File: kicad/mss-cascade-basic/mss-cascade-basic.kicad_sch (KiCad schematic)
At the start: 75 parts, among them J1 Screw_Terminal_01x02, U1 AP7381-50Y

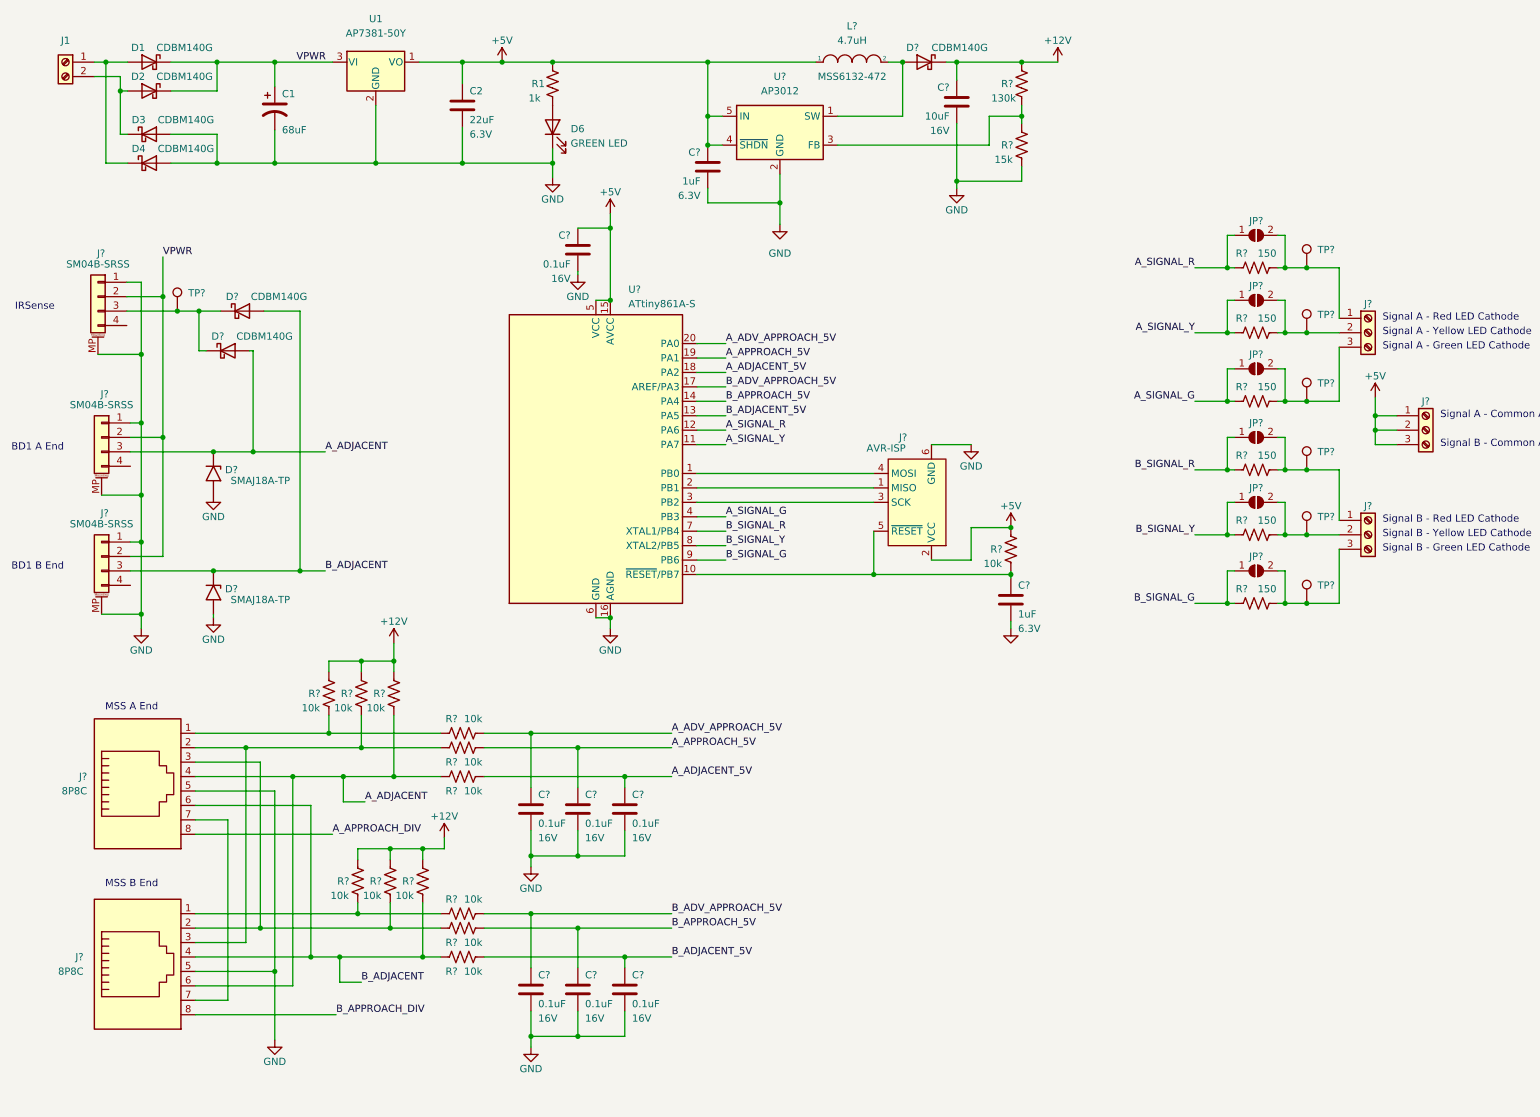
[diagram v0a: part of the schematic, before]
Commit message: Schematic updates and moving things around on the basic
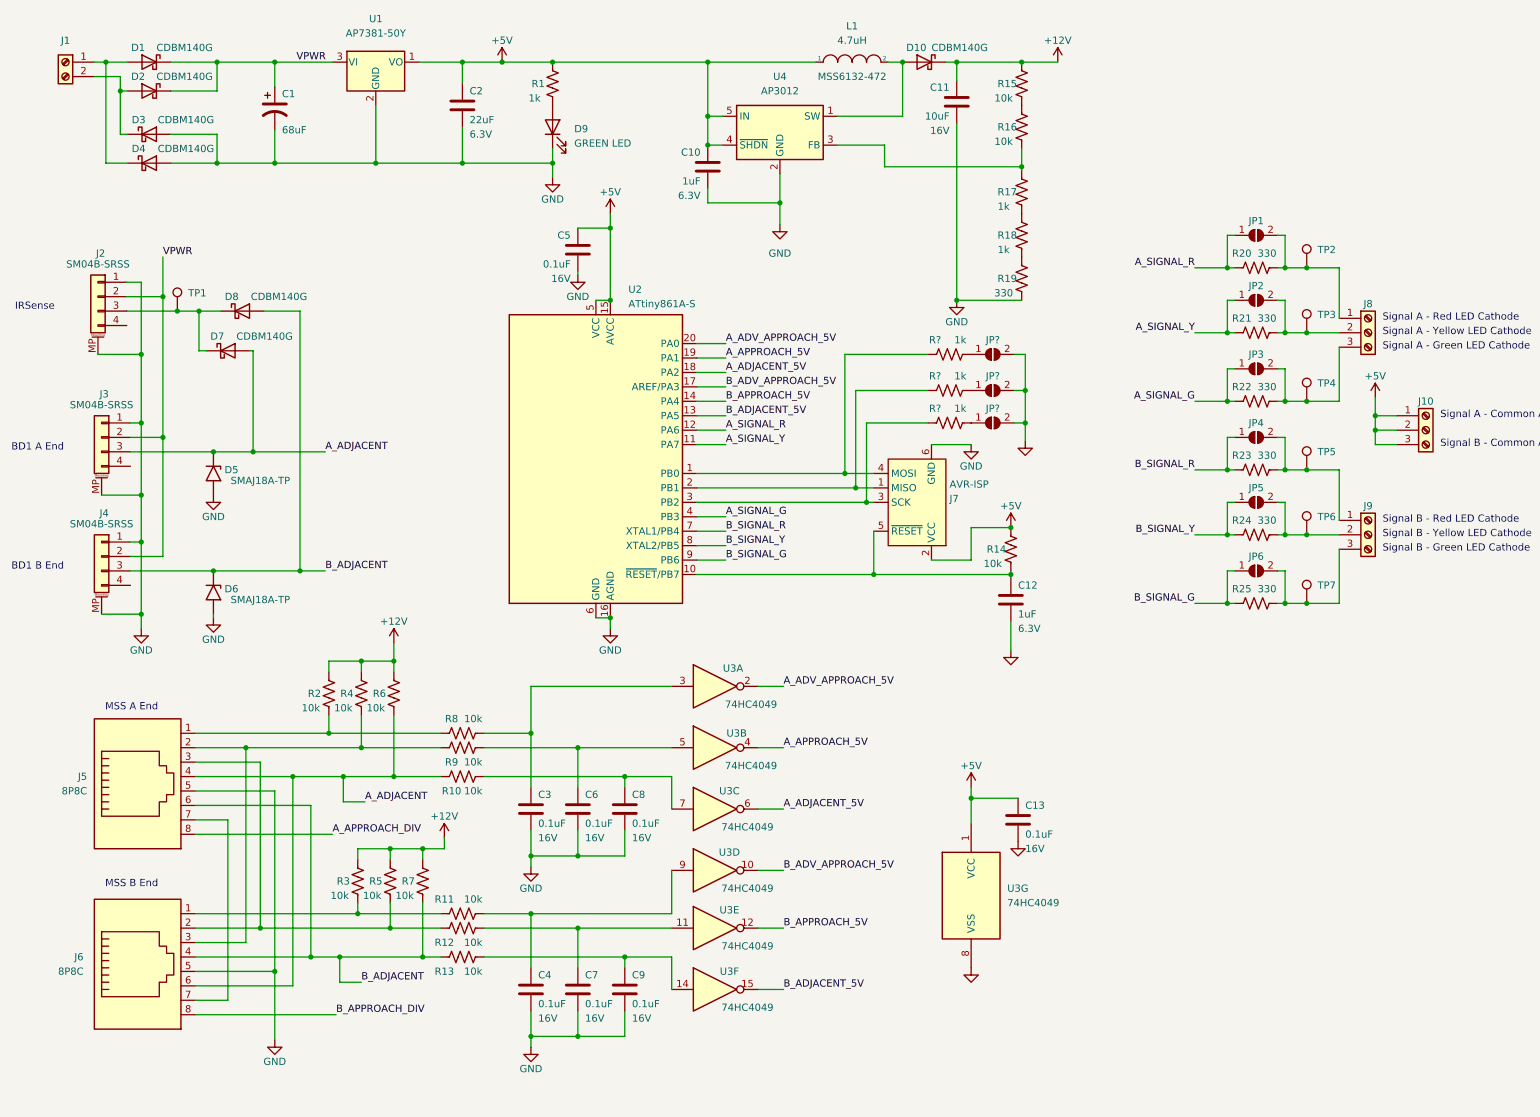
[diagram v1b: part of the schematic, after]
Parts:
- added C13: 0.1uF, Capacitor_SMD:C_0805_2012Metric, symbol Device:C
- added JP? (x3): SolderJumper_2_Open, Jumper:SolderJumper-2_P1.3mm_Open_RoundedPad1.0x1.5mm, symbol Jumper:SolderJumper_2_Open
- added R16: 10k, Resistor_SMD:R_0805_2012Metric, symbol Device:R_US
- added R17, R18, R? (x3): 1k, Resistor_SMD:R_0805_2012Metric, symbol Device:R_US
- added U3: 74HC4049, symbol 4xxx:4049
- R15: renamed from R?; value 130k -> 10k
- R19: renamed from R?; value 15k -> 330
- R20, R21, R22, R23, R24, R25: renamed from R?; value 150 -> 330
- gave numbers to parts that had none: 53
- renumbered D6 to D9
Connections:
- net +5V: now also C13.1, U3.1 (VCC)
- net A_ADJACENT_5V: now also U3.6; no longer C8.1, R10.1
- net A_ADV_APPROACH_5V: now also U3.2; no longer C3.1, R8.1
- net A_APPROACH_5V: now also U3.4; no longer C6.1, R9.1
- net B_ADJACENT_5V: now also U3.15; no longer C9.1, R13.1
- net B_ADV_APPROACH_5V: now also U3.10; no longer C4.1, R11.1
- net B_APPROACH_5V: now also U3.12; no longer C7.1, R12.1
- net GND: now also C13.2, JP?.2 (B), JP?.2 (B), JP?.2 (B), U3.8 (VSS)
- net at J7.4 (MOSI), U2.1 (PB0): now also R?.1
- net at J7.1 (MISO), U2.2 (PB1): now also R?.1
- net at J7.3 (SCK), U2.3 (PB2): now also R?.1
- new net: C7.1, R12.1, U3.11
- new net: JP?.1 (A), R?.2 (x3)
- new net: R18.1, R19.2
- new net: R17.1, R18.2
- new net: C9.1, R13.1, U3.14
- new net: C8.1, R10.1, U3.7
- new net: C3.1, R8.1, U3.3
- new net: C6.1, R9.1, U3.5
- new net: C4.1, R11.1, U3.9
- new net: R15.1, R16.2
- new net: R16.1, R17.2, U4.3 (FB)
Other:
- moved on the sheet: R19

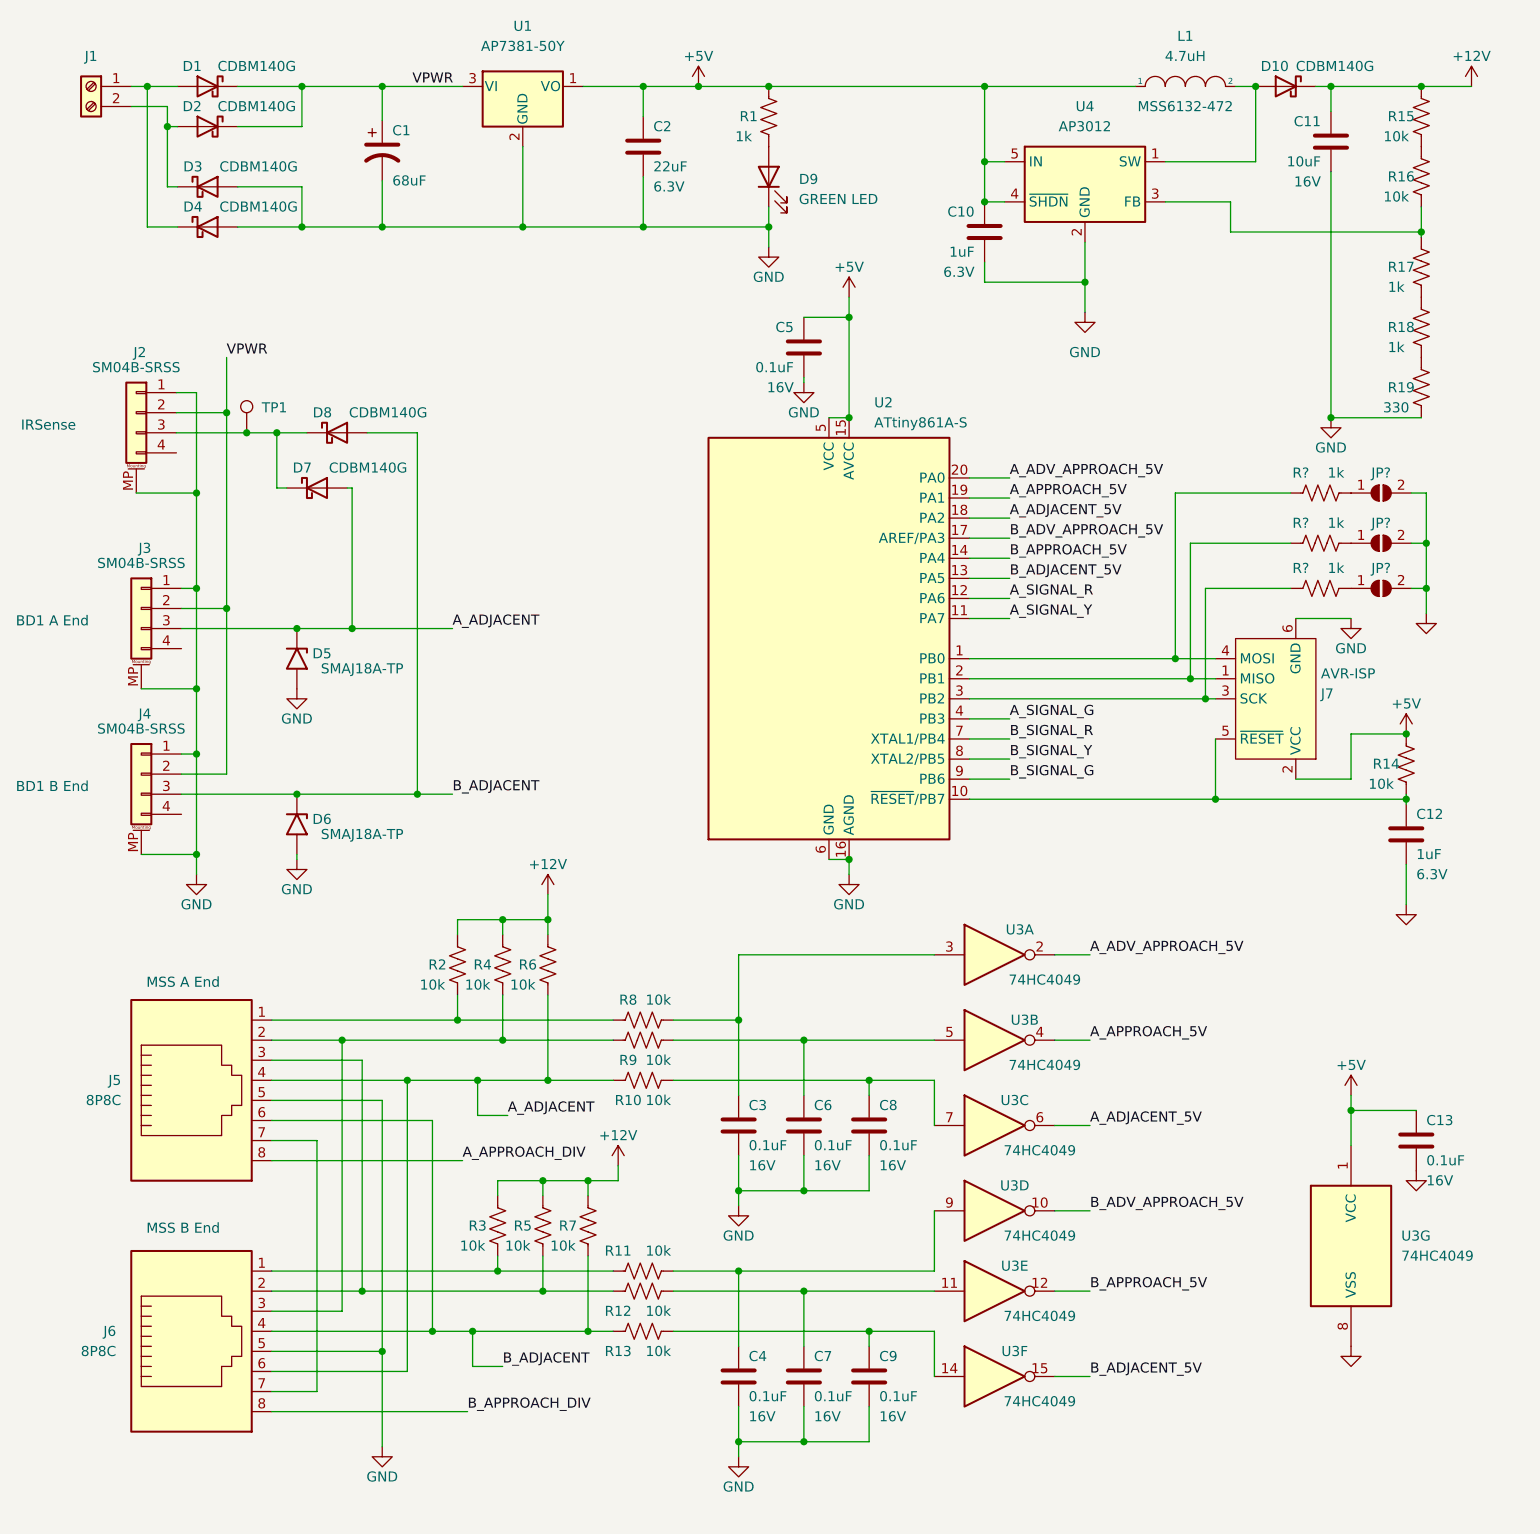
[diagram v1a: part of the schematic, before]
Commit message: Initial PCB layout for basic cascade
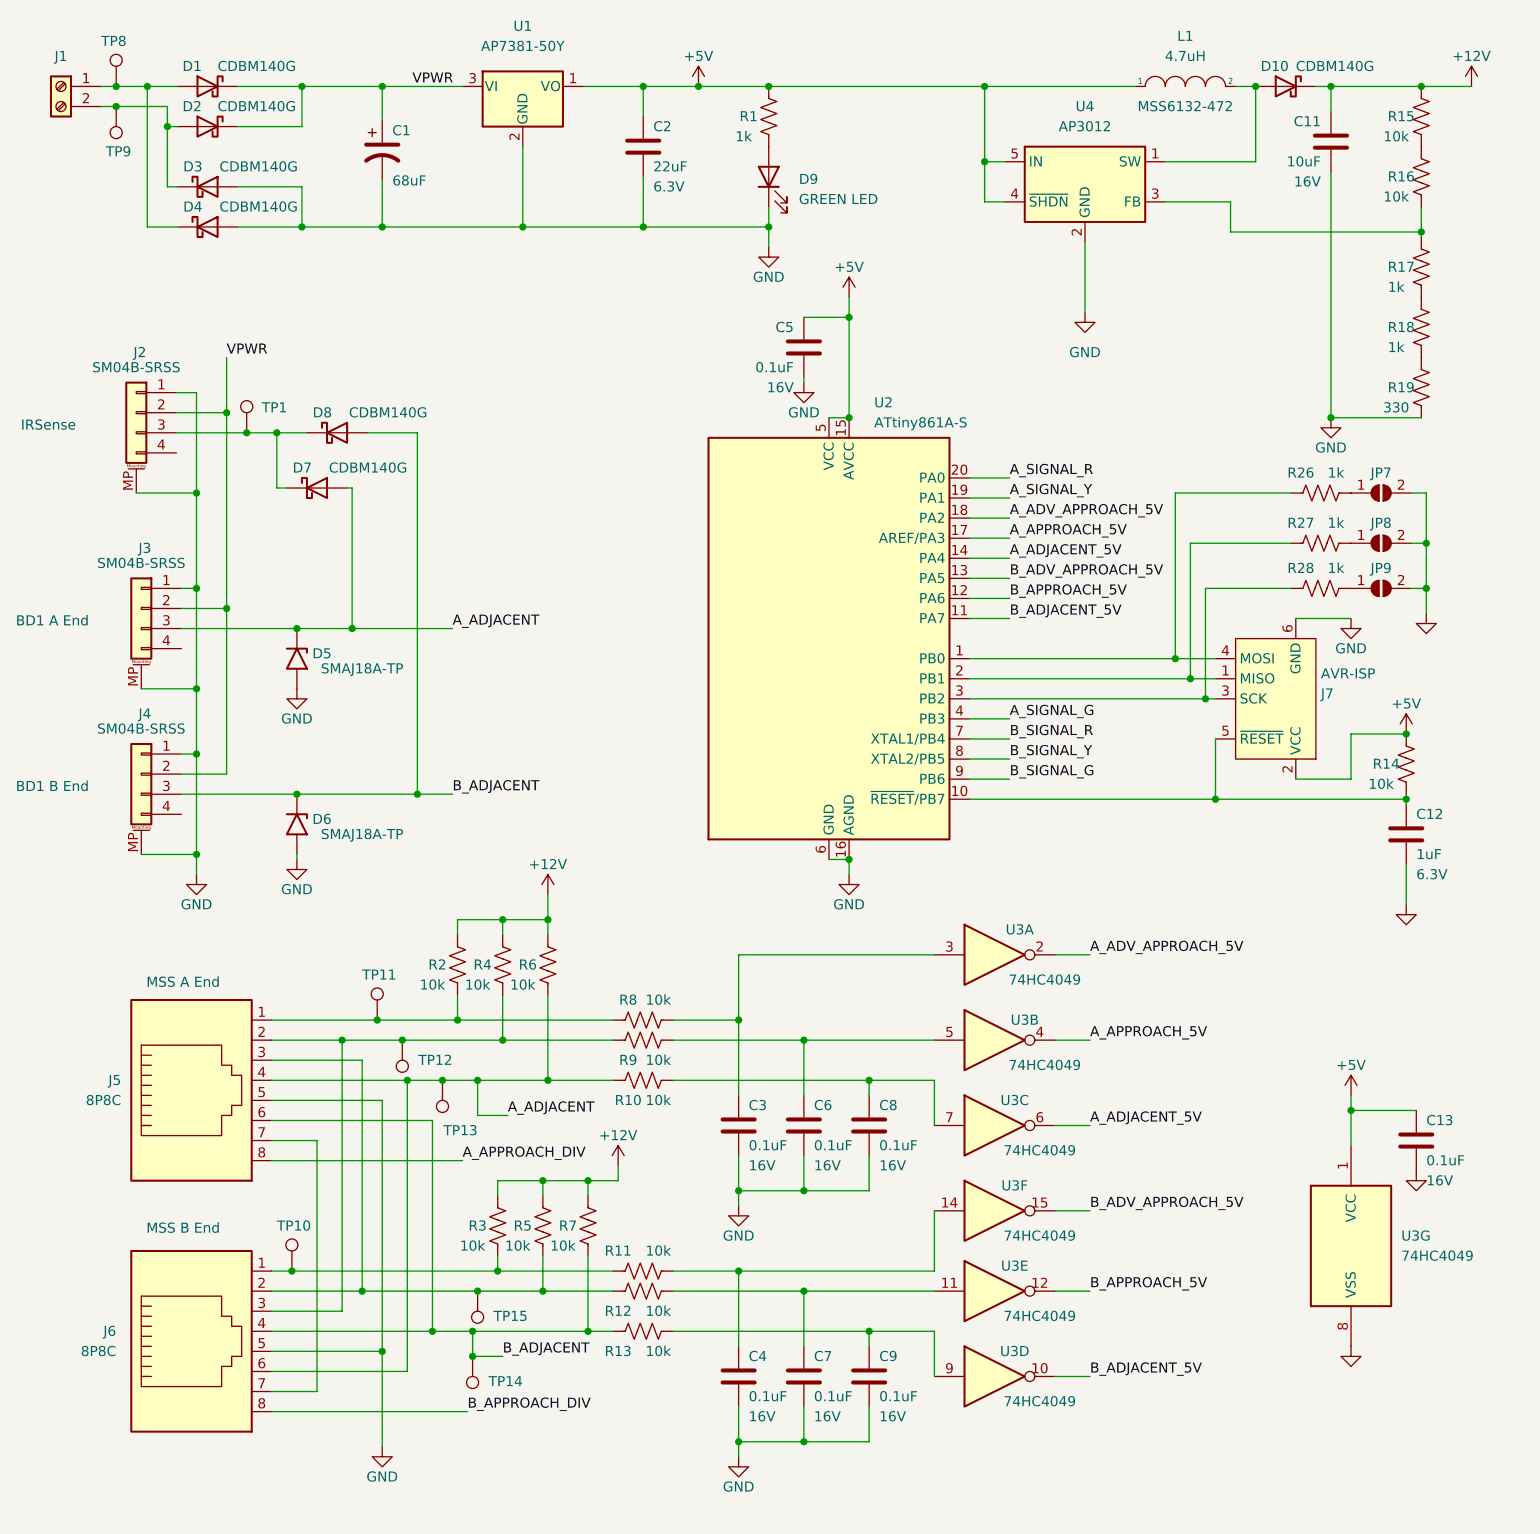
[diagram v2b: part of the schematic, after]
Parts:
- removed C10: 1uF, Capacitor_SMD:C_0805_2012Metric, symbol Device:C
- added TP10, TP11, TP12, TP13, TP14, TP15, TP8, TP9: TestPoint, TestPoint:TestPoint_Pad_D2.0mm, symbol Connector:TestPoint
- U3: footprint Package_SO:SO-16_3.9x9.9mm_P1.27mm -> (none)
- gave numbers to parts that had none: 6
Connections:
- net A_ADJACENT: now also TP13.1
- net A_ADJACENT_5V: now also U2.14 (PA4); no longer U2.18 (PA2)
- net A_ADV_APPROACH_5V: now also U2.18 (PA2); no longer U2.20 (PA0)
- net A_APPROACH_5V: now also U2.17 (AREF/PA3); no longer U2.19 (PA1)
- net A_SIGNAL_R: now also U2.20 (PA0); no longer U2.12 (PA6)
- net A_SIGNAL_Y: now also U2.19 (PA1); no longer U2.11 (PA7)
- net B_ADJACENT: now also TP14.1
- net B_ADJACENT_5V: now also U2.11 (PA7), U3.10; no longer U2.13 (PA5), U3.15
- net B_ADV_APPROACH_5V: now also U2.13 (PA5), U3.15; no longer U2.17 (AREF/PA3), U3.10
- net B_APPROACH_5V: now also U2.12 (PA6); no longer U2.14 (PA4)
- net at D1.2 (A), D4.1 (K), J1.1 (Pin_1): now also TP8.1
- net at J5.3, J6.2, R12.2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: now also TP15.1
- net at D2.2 (A), D3.1 (K), J1.2 (Pin_2): now also TP9.1
- net at C9.1, R13.1: now also U3.9; no longer U3.14
- net at J6.1, R11.2, R3.1: now also TP10.1
- net at J5.2, J6.3, R4.1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: now also TP12.1
- net at J5.1, R2.1, R8.2: now also TP11.1
- net at C4.1, R11.1: now also U3.14; no longer U3.9
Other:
- moved on the sheet: J1
